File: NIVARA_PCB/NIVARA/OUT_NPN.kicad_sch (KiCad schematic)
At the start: 0 parts

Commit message: ACTUALIZACION DE SALIDAS NPN Y PNP
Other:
- added sheet O_NPN (O_NPN.kicad_sch)
- added sheet O_NPN1 (O_NPN.kicad_sch)
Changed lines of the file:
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@@
 	(generator_version "9.0")
 	(paper "A4")
+	(wire
+		(pts
+			(xy 41.91 95.25) (xy 46.99 95.25)
+		)
+		(stroke
+			(width 0)
+			(type default)
+		)
+	)
+	(wire
+		(pts
+			(xy 76.2 69.85) (xy 80.01 69.85)
+		)
+		(stroke
+			(width 0)
+			(type default)
+		)
+	)
+	(wire
+		(pts
+			(xy 43.18 69.85) (xy 46.99 69.85)
+		)
+		(stroke
+			(width 0)
+			(type default)
+		)
+	)
+	(wire
+		(pts
+			(xy 76.2 95.25) (xy 80.01 95.25)
+		)
+		(stroke
+			(width 0)
+			(type default)
+		)
+	)
 	(hierarchical_label "IN_1"
 		(shape input)
-		(at 170.18 57.15 180)
+		(at 43.18 69.85 180)
 		(effects
 			(font
@@
 	(hierarchical_label "OUT_2"
 		(shape output)
-		(at 191.77 64.77 0)
-		(effects
-			(font
-				(size 1.27 1.27)
-			)
-			(justify left)
-		)
-	)
-	(hierarchical_label "OUT_1"
-		(shape output)
-		(at 191.77 57.15 0)
+		(at 80.01 95.25 0)
 		(effects
 			(font
@@
 	(hierarchical_label "IN_2"
 		(shape input)
-		(at 170.18 64.77 180)
+		(at 41.91 95.25 180)
 		(effects
 			(font
@@
 		)
 	)
+	(hierarchical_label "OUT_1"
+		(shape output)
+		(at 80.01 69.85 0)
+		(effects
+			(font
+				(size 1.27 1.27)
+			)
+			(justify left)
+		)
+	)
+	(sheet
+		(at 46.99 62.23)
+		(size 29.21 16.51)
+		(exclude_from_sim no)
+		(in_bom yes)
+		(on_board yes)
+		(dnp no)
+		(fields_autoplaced yes)
+		(stroke
+			(width 0.1524)
+			(type solid)
+		)
+		(fill
+			(color 0 0 0 0.0000)
+		)
+		(property "Sheetname" "O_NPN"
+			(at 46.99 61.5184 0)
+			(effects
+				(font
+					(size 1.27 1.27)
+				)
+				(justify left bottom)
+			)
+		)
+		(property "Sheetfile" "O_NPN.kicad_sch"
+			(at 46.99 79.3246 0)
+			(effects
+				(font
+					(size 1.27 1.27)
+				)
+				(justify left top)
+			)
+		)
+		(pin "OUT" input
+			(at 76.2 69.85 0)
+			(effects
+				(font
+					(size 1.27 1.27)
+				)
+				(justify right)
+			)
+		)
+		(pin "IN" input
+			(at 46.99 69.85 180)
+			(effects
+				(font
+					(size 1.27 1.27)
+				)
+				(justify left)
+			)
+		)
+		(instances
+			(project "NIVARA"
+				(path "/6298d7d5-28da-40bf-9586-24a8e5c02b82/7ff0dada-fc46-483c-91ad-b264be8c64cf/e83b750d-d99e-4d1f-827c-e43e7f4ff994"
+					(page "26")
+				)
+			)
+		)
+	)
+	(sheet
+		(at 46.99 87.63)
+		(size 29.21 16.51)
+		(exclude_from_sim no)
+		(in_bom yes)
+		(on_board yes)
+		(dnp no)
+		(fields_autoplaced yes)
+		(stroke
+			(width 0.1524)
+			(type solid)
+		)
+		(fill
+			(color 0 0 0 0.0000)
+		)
+		(property "Sheetname" "O_NPN1"
+			(at 46.99 86.9184 0)
+			(effects
+				(font
+					(size 1.27 1.27)
+				)
+				(justify left bottom)
+			)
+		)
+		(property "Sheetfile" "O_NPN.kicad_sch"
+			(at 46.99 104.7246 0)
+			(effects
+				(font
+					(size 1.27 1.27)
+				)
+				(justify left top)
+			)
+		)
+		(pin "OUT" input
+			(at 76.2 95.25 0)
+			(effects
+				(font
+					(size 1.27 1.27)
+				)
+				(justify right)
+			)
+		)
+		(pin "IN" input
+			(at 46.99 95.25 180)
+			(effects
+				(font
+					(size 1.27 1.27)
+				)
+				(justify left)
+			)
+		)
+		(instances
+			(project "NIVARA"
+				(path "/6298d7d5-28da-40bf-9586-24a8e5c02b82/7ff0dada-fc46-483c-91ad-b264be8c64cf/e83b750d-d99e-4d1f-827c-e43e7f4ff994"
+					(page "25")
+				)
+			)
+		)
+	)

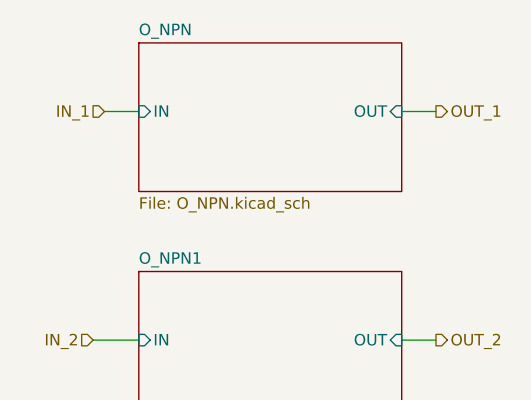
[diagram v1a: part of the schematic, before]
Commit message: arreglo del desastre que tenia con las salidas PNP
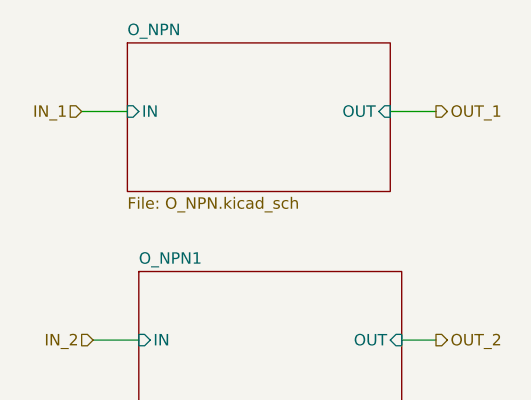
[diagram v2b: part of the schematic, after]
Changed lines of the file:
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@@
 	(wire
 		(pts
-			(xy 76.2 69.85) (xy 80.01 69.85)
+			(xy 74.93 69.85) (xy 80.01 69.85)
 		)
 		(stroke
@@
 	(wire
 		(pts
-			(xy 43.18 69.85) (xy 46.99 69.85)
+			(xy 40.64 69.85) (xy 45.72 69.85)
 		)
 		(stroke
@@
 	(hierarchical_label "IN_1"
 		(shape input)
-		(at 43.18 69.85 180)
+		(at 40.64 69.85 180)
 		(effects
 			(font
@@
 	)
 	(sheet
-		(at 46.99 62.23)
+		(at 45.72 62.23)
 		(size 29.21 16.51)
 		(exclude_from_sim no)
@@
 		)
 		(property "Sheetname" "O_NPN"
-			(at 46.99 61.5184 0)
+			(at 45.72 61.5184 0)
 			(effects
 				(font
@@
 		)
 		(property "Sheetfile" "O_NPN.kicad_sch"
-			(at 46.99 79.3246 0)
+			(at 45.72 79.3246 0)
 			(effects
 				(font
@@
 		)
 		(pin "OUT" input
-			(at 76.2 69.85 0)
+			(at 74.93 69.85 0)
 			(effects
 				(font
@@
 		)
 		(pin "IN" input
-			(at 46.99 69.85 180)
+			(at 45.72 69.85 180)
 			(effects
 				(font
